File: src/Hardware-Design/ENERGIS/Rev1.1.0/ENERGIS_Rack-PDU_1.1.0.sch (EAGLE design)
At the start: 430 parts, among them IC1 MP2315GJ-Z, IC10 HLW8032, IC11 HLW8032, IC12 HLW8032, IC13 MP150GJ, IC14 HLW8032, IC15 RP2040, IC16 HLW8032, IC17 MCP6001RT-I/OT, IC18 W25Q128JVPIQ, IC19 CAT24C256HU4IGT3, IC2 MP2315GJ-Z, IC20 W5500, IC21 DNI, IC22 MCP6001RT-I/OT, IC3 ULN2803AFWG, IC4 MCP23017T-E/ML, IC5 MP150GJ, IC6 HLW8032, IC7 HLW8032, IC8 HLW8032, IC9 SN74HC151PWR, J10 0R 1%, J2 JP, J7 JP, J8 0R 1%, J9 0R 1%, K1 G2RL-1A-E DC12, K2 G2RL-1A-E DC12, K3 G2RL-1A-E DC12, K4 G2RL-1A-E DC12, K5 G2RL-1A-E DC12, K6 G2RL-1A-E DC12, K7 G2RL-1A-E DC12, K8 G2RL-1A-E DC12, P12ON Green, P3ON Green, P5ON DNI, SW3 DNI, T1 BSS138, X1 12MHz, X2 25MHz

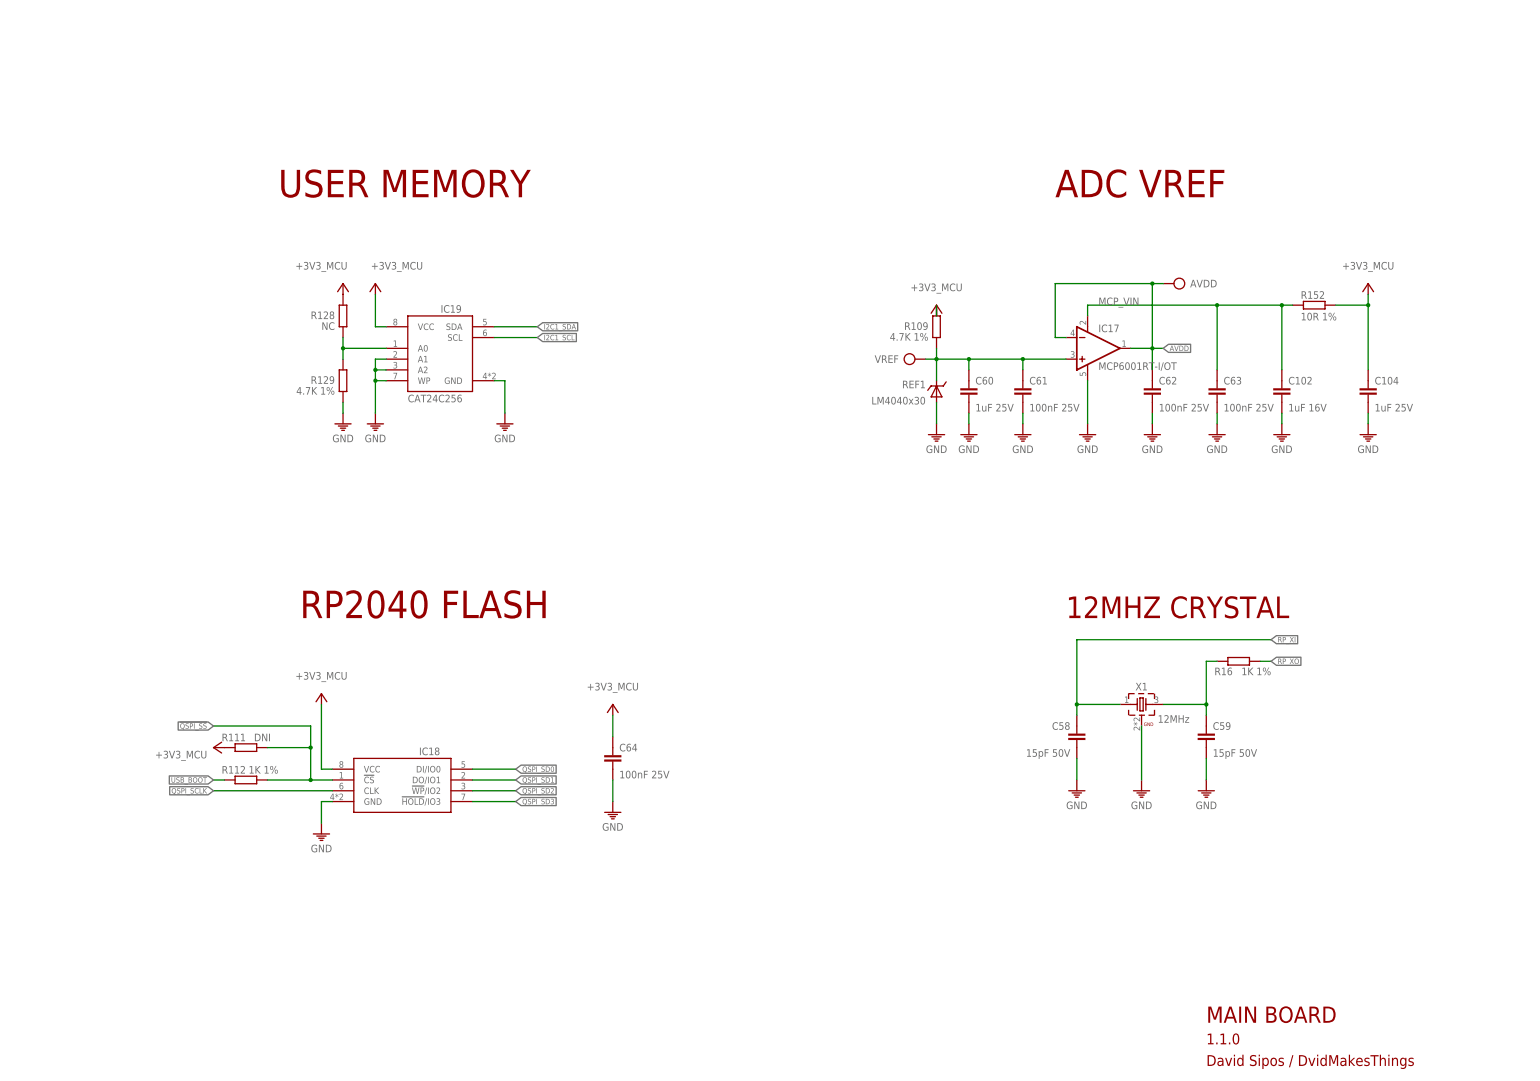
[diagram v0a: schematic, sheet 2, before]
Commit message: major pre-release update on project files and documentation
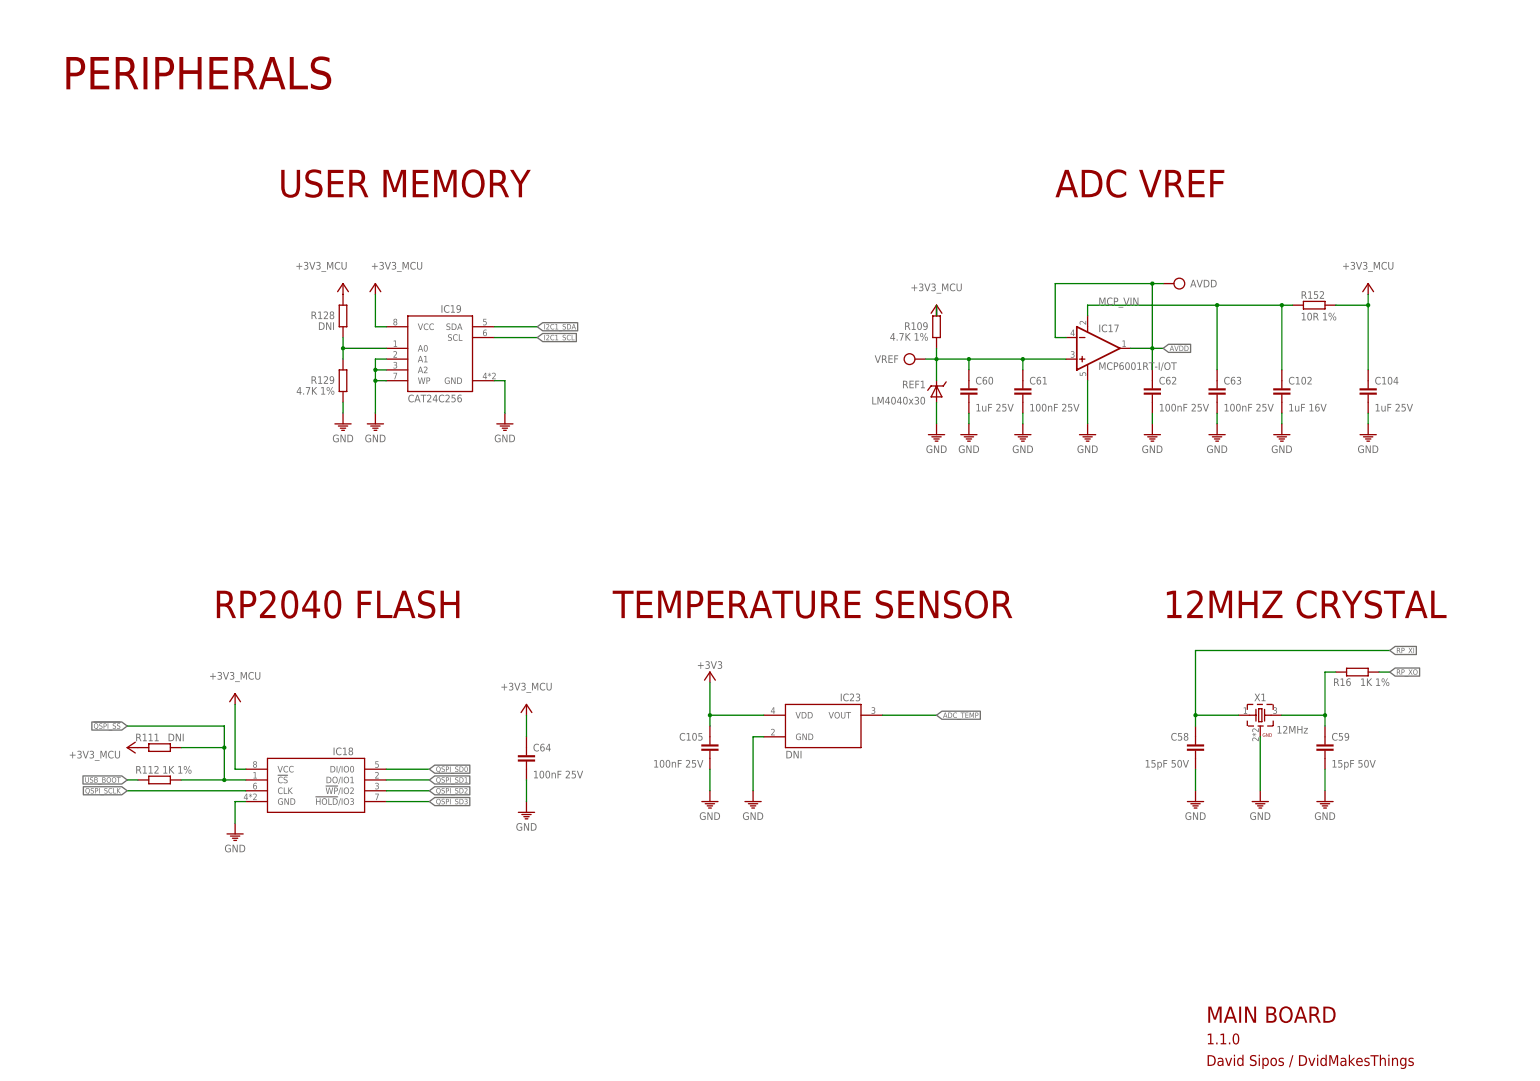
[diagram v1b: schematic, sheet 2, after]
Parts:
- added C105: 100nF 25V, ds_capacitors:100NF-25V-0201
- added IC23: DNI, ds_ic_peripherals:MCP9700AT-E/LT
- added R172: DNI, ds_passive:R0402
- AC_L, AC_N: value MOUNT-PAD-ROUND3.0 -> FASTON-1217861-1; device holes:MOUNT-PAD-ROUND3.0 -> ds_con:FASTON-1217861-1
- C1, C14, C17: value DNI -> 22uF 25V
- C100, C3, C6, C8, C98: value DNI -> 100nF 25V
- C11: value DNI -> 33pF 50V
- C83: value C1206C102KGRACTM -> 1NF-2KV; device ds_passive:C-1206 -> ds_capacitors:1NF-2KV
- C97, C99: value DNI -> 10uF 50V
- FAN, GDRC, RGTG: value (none) -> DNI
- IC9: value SN74HC151PWR -> CD74ACT151M96; device ds_ic_logic:SN74HC151PWR -> ds_ic_logic:74AC151
- J2, J7: value JP -> DNI
- L1: device ds_passive:L -> ds_inductor:4.7UH
- L2: value 4.2uH -> 4.7uH; device ds_passive:L -> ds_inductor:4.2UH
- L_OUT1, L_OUT2, L_OUT3, L_OUT4, L_OUT5, L_OUT6, L_OUT7, L_OUT8, N_OUT1, N_OUT2, N_OUT3, N_OUT4, N_OUT5, N_OUT6, N_OUT7, N_OUT8: value MOUNT-PAD-ROUND2.8 -> FASTON-1217861-1; device holes:MOUNT-PAD-ROUND2.8 -> ds_con:FASTON-1217861-1
- R10: value 33K -> 33K 1%; device ds_passive:R0402 -> ds_resistor:33K-1%0402
- R11: value DNI -> 40.2K 1%
- R12: value DNI -> 7.5K 1%
- R128, R165: value NC -> DNI
- R143: device ds_passive:R0201 -> ds_resistor:12.4K-1%0201
- R148: value DNI -> 2.4K 1%
- R162: value DNI -> 10K 1%
- R170: value DNI -> 0R 1%
- R3: value DNI -> 100K 1%
- R4: value DNI -> 9.09K 1%
- R7: value DNI -> 10R 1%
- R8: value DNI -> 20K 1%
- renumbered BOOT to BT, RESET to RES, RX1 to TX0
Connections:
- new net 3V3_EN: IC2.EN, R171.1, R172.1, R2.2
- new net ADC_TEMP: IC15.GPIO27/ADC1, IC23.VOUT
- net +3V3: now also C105.1, IC23.VDD
- net BUCK_EN: now also R172.2; no longer IC2.EN, R171.1, R2.2
- net FAN_CTRL: now also IC15.GPIO22; no longer IC15.GPIO27/ADC1
- net GND: now also C105.2, IC23.GND
- net LCD_RES: no longer IC15.GPIO22
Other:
- note added: "TEMPERATURE SENSOR"
- moved on the sheet: C58, C59, C64, IC18, R111, R112, R16, X1

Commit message: update documentation
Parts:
- added 3V3A, ADCUSB, ADC_TEMP, BOOT, FCTL, MCPVIN, RST, UTX: DNI, ds_passive:TP-ROUND
- added DNI: 0R 1%, ds_resistor:0R0402
- C83: value 1NF-2KV -> 1nF 2kV
- IC1: value MP2315GJ-Z -> DNI
- L2: value 4.7uH -> 4.7uH 3.5A
- R170: value 0R 1% -> DNI
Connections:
- net +3V3_A: now also 3V3A.P$1
- net ADC_TEMP: now also ADC_TEMP.P$1
- net ADC_V_USB: now also ADCUSB.P$1
- net AVDD: now also DNI.1
- net FAN_CTRL: now also FCTL.P$1
- net MCP_VIN: now also DNI.2, MCPVIN.P$1
- net RUN: now also RST.P$1
- net TX_OUTSEL: now also UTX.P$1
- net USB_BOOT: now also BOOT.P$1
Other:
- moved on the sheet: C102, C104, R126, R127, R132, R152, R170, RES

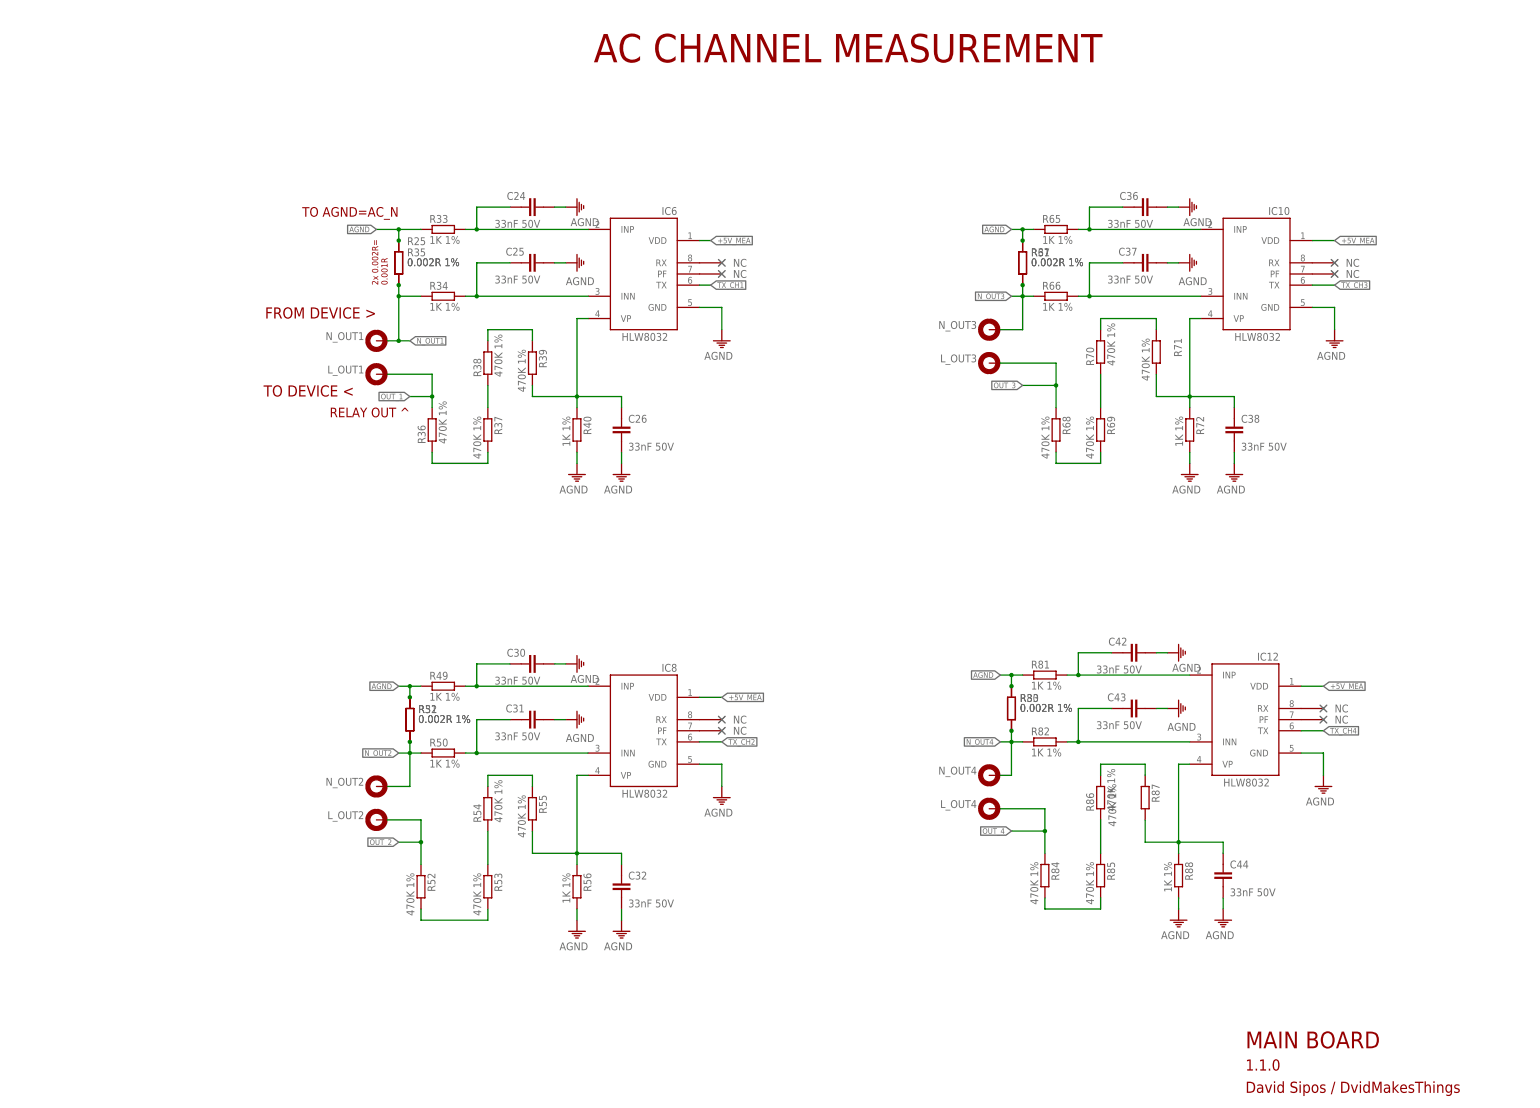
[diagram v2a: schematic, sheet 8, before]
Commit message: correct BOM
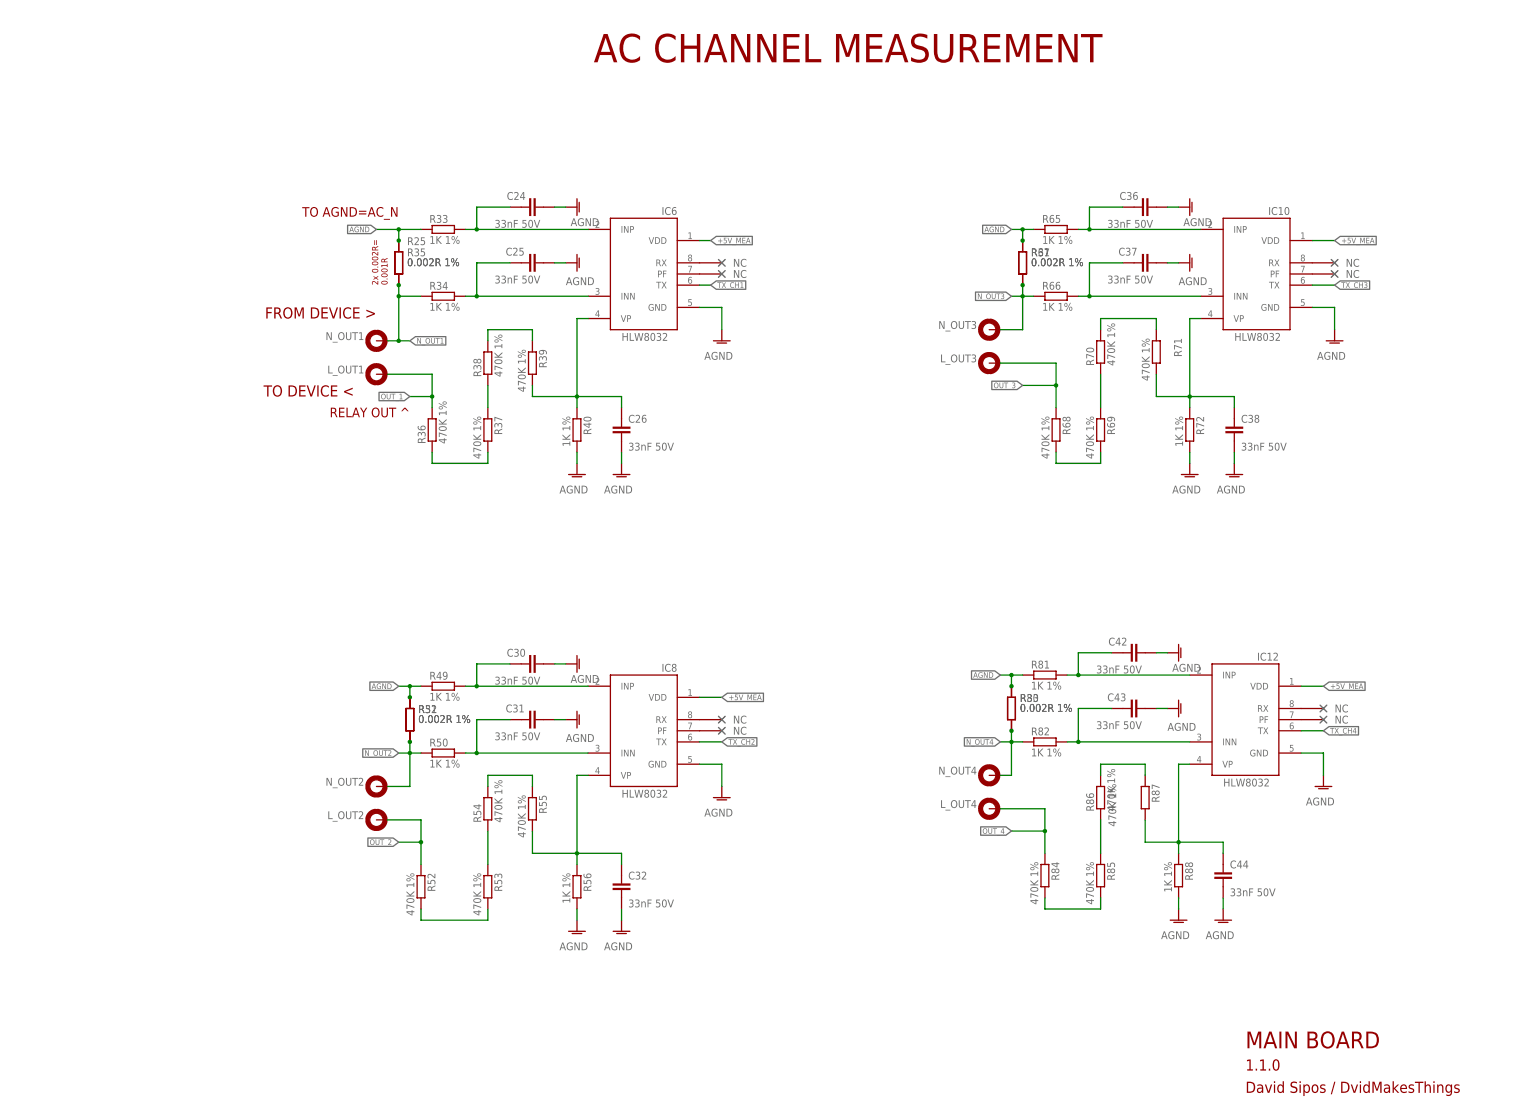
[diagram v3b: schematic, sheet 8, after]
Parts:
- IC21: value DNI -> MIC5504-3.3YM5
- IC23: value DNI -> MCP9700AT-E/LT
- IC9: value CD74ACT151M96 -> SN74HC151PWR
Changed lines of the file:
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@@
 <part name="R64" library="ds_resistor" deviceset="1K-1%_ARRAY" device="0603X4-1206" package3d_urn="urn:adsk.eagle:package:49287421/2" value="1K 1%"/>
 <part name="GND25" library="ds_passive" deviceset="GND" device=""/>
-<part name="IC9" library="ds_ic_logic" deviceset="74AC151" device="" package3d_urn="urn:adsk.eagle:package:16485/2" value="CD74ACT151M96"/>
+<part name="IC9" library="ds_ic_logic" deviceset="74AC151" device="" package3d_urn="urn:adsk.eagle:package:16485/2" value="SN74HC151PWR"/>
 <part name="+3V1" library="ds_passive" deviceset="+3V3" device=""/>
 <part name="C33" library="ds_capacitors" deviceset="100NF-25V" device="-0402" package3d_urn="urn:adsk.eagle:package:46766485/4" value="100nF 25V"/>
@@
 <part name="+3V24" library="ds_passive" deviceset="+3V3" device=""/>
 <part name="P+15" library="ds_passive" deviceset="+5V" device=""/>
-<part name="IC21" library="ds_ic_vreg" deviceset="MIC5504-3.3YM5-TR" device="" package3d_urn="urn:adsk.eagle:package:25419215/2" value="DNI"/>
+<part name="IC21" library="ds_ic_vreg" deviceset="MIC5504-3.3YM5-TR" device="" package3d_urn="urn:adsk.eagle:package:25419215/2" value="MIC5504-3.3YM5 "/>
 <part name="C97" library="ds_capacitors" deviceset="10UF-50V" device="-0805" package3d_urn="urn:adsk.eagle:package:46766483/3" value="10uF 50V"/>
 <part name="C98" library="ds_capacitors" deviceset="100NF-25V" device="-0201" package3d_urn="urn:adsk.eagle:package:47403530/3" value="100nF 25V"/>
@@
 <part name="R170" library="ds_resistor" deviceset="0R" device="1206" package3d_urn="urn:adsk.eagle:package:46683745/2" value="DNI"/>
 <part name="R171" library="ds_resistor" deviceset="10K-1%" device="0402" package3d_urn="urn:adsk.eagle:package:46683744/3" value="10K 1%"/>
-<part name="IC23" library="ds_ic_peripherals" deviceset="MCP9700" device="AT-E/LT" package3d_urn="urn:adsk.eagle:package:49052119/1" value="DNI"/>
+<part name="IC23" library="ds_ic_peripherals" deviceset="MCP9700" device="AT-E/LT" package3d_urn="urn:adsk.eagle:package:49052119/1" value="MCP9700AT-E/LT "/>
 <part name="C105" library="ds_capacitors" deviceset="100NF-25V" device="-0201" package3d_urn="urn:adsk.eagle:package:47403530/3" value="100nF 25V"/>
 <part name="GND94" library="ds_passive" deviceset="GND" device=""/>
